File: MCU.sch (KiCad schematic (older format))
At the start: 36 parts, among them P1 CONN_02X05, P2 USB_OTG, SW48 Reset, U1 IS31FL3732, U2 MK20DX256VLH7, X1 CRYSTAL_SMD

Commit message: Reworked the Board
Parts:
- removed C13, C18, C19, C2, C3: 1uF, Capacitors_SMD:C_0603, symbol CP1
- removed C14, C15, C17, C20, C21, C4, C5, C6, C7: 0.1uF, Capacitors_SMD:C_0603, symbol CP1
- removed C8: 2.2uF, Capacitors_SMD:C_0603, symbol CP1
- removed D48: LED, LEDs:LED_0805, symbol LED
- removed P1: CONN_02X05, Pin_Headers:Pin_Header_Straight_2x05, symbol CONN_02X05
- removed P2: USB_OTG, Connect:USB_Micro-B, symbol USB_OTG
- removed SW48: Reset, mx2a:KSEM31GLFS, symbol SW_PUSH
- removed U1: IS31FL3732, Housings_DFN_QFN:UQFN-40-1EP_5x5mm_Pitch0.4mm, symbol IS31FL3732
- removed U2: MK20DX256VLH7, Housings_QFP:LQFP-64_10x10mm_Pitch0.5mm, symbol MK20DX256VLH7
- added C11, C13, C3, C6: 0.1uF, Capacitors_SMD:C_0603, symbol C
- added C2, C5, C7: 1uF, Capacitors_SMD:C_0603, symbol C
- added C4: 100uF, Capacitors_SMD:C_1206, symbol C
- added C8: 2.2uF, Capacitors_SMD:C_0603, symbol C
- added LED48: LED, lib.pretty:LED_0805, symbol LED
- added P1: USB_OTG, lib.pretty:Micro-USB_629105150521, symbol USB_OTG
- added P2, P3, P5: CONN_01X04, lib.pretty:Conn-4, symbol CONN_01X04
- added P4: FLASH_HDR, lib.pretty:JLINK_NEEDLE, symbol FLASH_HDR
- added P6, P7: CONN_01X02, lib.pretty:Conn-2, symbol CONN_01X02
- added R11: 100, Resistors_SMD:R_0603, symbol R
- added SW48: TAC_SWITCH, lib.pretty:PTS810, symbol TAC_SWITCH
- added U1: IS31FL3737, Housings_DFN_QFN:UQFN-40-1EP_5x5mm_Pitch0.4mm, symbol IS31FL3737
- added U2: MK20DX256VLH7-RESCUE-RainbowFox, Housings_QFP:LQFP-64_10x10mm_Pitch0.5mm, symbol MK20DX256VLH7-RESCUE-RainbowFox
- C1: value 100uF -> 0.1uF; footprint Capacitors_SMD:C_0805 -> Capacitors_SMD:C_0603
- C12: value 100n -> 0.1uF
- C9: value 2.2uF -> 0.1uF
- R1: value 1k -> 100k
- R3: value 33 -> 4.7k
- R4: value 33 -> 100k
- R5: value 5M -> 4.7k; footprint Resistors_SMD:R_0805 -> Resistors_SMD:R_0603
- R6: value 20k -> 33
- R7: value 1k -> 33
- R8: value 1k -> 20k
- R9: value 100k -> 5M; footprint Resistors_SMD:R_0603 -> Resistors_SMD:R_0805
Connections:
- net +3V3: now also C1.1, C9.1, R2.1, R3.1, R5.1, C11.1, C13.1, C2.1, C8.1, P4.1 (VCCS), U1.32 (VIO), U2.3 (VDD), U2.30 (VDD), U2.48 (VDD), U2.7 (VOUT33); no longer C9.2, R7.2, R8.2
- net +5V: now also C10.1, C3.1, C4.1, C5.1, C6.1, C7.1, P1.1 (VBUS), P2.1 (P1), P3.4 (P4), P4.5 (VKS), U1.19 (PVCC), U1.26 (PVCC), U1.31 (VCC), U2.8 (VREGIN); no longer C1.2, C10.2
- net D+: now also R7.1, U2.5 (USB0_DP); no longer R4.2
- net D-: now also R6.1, U2.6 (USB0_DM); no longer R3.2
- net GND: now also C1.2, C10.2, C9.2, R1.1, R4.1, R8.2, R9.2, C11.2, C13.2, C2.2, C3.2, C4.2, C5.2, C6.2, C7.2, P1.5 (GND), P2.4 (P4), P3.2 (P2), P4.3 (GND), SW48.4, U1.11 (PGND), U1.29 (AGND), U1.36 (ADDR), U1.4 (PGND), U1.40 (GND), U1.41 (Pad), U2.31 (VSS), U2.4 (VSS), U2.47 (VSS); no longer C1.1, C10.1, R1.2, R5.2, R6.1, R9.1
- net INTB: now also R2.2, P5.1 (P1), U1.37 (INTB), U2.40 (PTB17); no longer R2.1
- net MCU_RESET: now also P4.10 (RES), SW48.2, U2.34 (RESET_b)
- net PTA5: now also P4.9 (TRST), U2.27 (PTA5)
- net RX0: now also P4.8 (TDI), U2.23 (PTA1)
- net SCL: now also R3.2, P5.4 (P4), U1.35 (SCL), U2.35 (PTB0/LLWU_P5); no longer R7.1
- net SDA: now also R5.2, P5.3 (P3), U1.34 (SDA), U2.36 (PTB1); no longer R8.1
- net SDB: now also R1.2, P5.2 (P2), U1.38 (SDB), U2.39 (PTB16); no longer R9.2
- net SWD_CLK: now also R10.2, P3.3 (P3), P4.4 (TCK); no longer R10.1
- net TX0: now also P4.6 (TDO), U2.24 (PTA2/TRACE_SWD)
- net R_Ext renamed USB_D-
- net USB_D-: now also P1.2 (D-), P2.2 (P2)
- net X+: no longer names the net of X1.1
- net X+: now also U2.32 (EXTAL0/PTA18)
- net X-: no longer names the net of X1.2
- net X-: now also U2.33 (XDAL0/PTA19)
- new net: C8.2, R9.1
- new net: R11.1, U2.25 (PTA3/SWD_DIO)
- new net: R10.1, U2.22 (PTA0/SWD_CLK)
- new net: R4.2, U1.39 (IICRST)
- new net: R8.1, U1.30 (RSET)
- new net CS1: U1.15 (CS1)
- new net CS10: U1.25 (CS10)
- new net CS11: U1.27 (CS11)
- new net CS12: U1.28 (CS12)
- new net CS2: U1.16 (CS2)
- new net CS3: U1.17 (CS3)
- new net CS4: U1.18 (CS4)
- new net CS5: U1.20 (CS5)
- new net CS6: U1.21 (CS6)
- new net CS7: U1.22 (CS7)
- new net CS8: U1.23 (CS8)
- new net CS9: U1.24 (CS9)
- new net PTA12: U2.28 (PTA12)
- new net PTA13: U2.29 (PTA13/LLWU_P4)
- new net PTA4: U2.26 (PTA4/LLWU_P3)
- new net PTB18: U2.41 (PTB18)
- new net PTB19: U2.42 (PTB19)
- new net PTB2: U2.37 (PTB2)
- new net PTB3: U2.38 (PTB3)
- new net PTC0: U2.43 (PTC0)
- new net PTC1: U2.44 (PTC1/LLWU_P6)
- new net PTC10: U2.55 (PTC10)
- new net PTC11: U2.56 (PTC11/LLWU_P11)
- new net PTC2: U2.45 (PTC2)
- new net PTC3: U2.46 (PTC3/LLWU_P7)
- new net PTC4: U2.49 (PTC4/LLWU_P8)
- new net PTC5: U2.50 (PTC5/LLWU_P9)
- new net PTC6: U2.51 (PTC6/LLWU_P10)
- new net PTC7: U2.52 (PTC7)
- new net PTC8: U2.53 (PTC8)
- new net PTC9: U2.54 (PTC9)
- new net PTD0: U2.57 (PTD0/LLWU_P12)
- new net PTD1: U2.58 (PTD1)
- new net PTD4: U2.61 (PTD4/LLWU_P14)
- new net PTD5: U2.62 (PTD5)
- new net PTD6: U2.63 (PTD6/LLWU_P15)
- new net PTD7: U2.64 (PTD7)
- new net RX1: P7.1 (P1), U2.1 (PTE0)
- new net RX2: P6.1 (P1), U2.59 (PTD2/LLWU_P13)
- new net SW1: U1.1 (SW1)
- new net SW10: U1.12 (SW10)
- new net SW11: U1.13 (SW11)
- new net SW12: U1.14 (SW12)
- new net SW2: U1.2 (SW2)
- new net SW3: U1.3 (SW3)
- new net SW4: U1.5 (SW4)
- new net SW5: U1.6 (SW5)
- new net SW6: U1.7 (SW6)
- new net SW7: U1.8 (SW7)
- new net SW8: U1.9 (SW8)
- new net SW9: U1.10 (SW9)
- new net SWD_DIO: P3.1 (P1), P4.2 (TMS), R11.2
- new net TX1: P7.2 (P2), U2.2 (PTE1/LLWU_P0)
- new net TX2: P6.2 (P2), U2.60 (PTD3)
- new net USB_D+: P1.3 (D+), P2.3 (P3), R7.2
- no-connect marks 41 -> 19
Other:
- note added: "RESET internally\npulled high"

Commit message: Performed the changes from https://github.com/Project-Aurora/RainbowFox/commit/d956c5c3914152606eb0eeb9caeb00dc6e36fd84
Added Resistor to ground for firmware-LED
Connect VBAT to 3.3V
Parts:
- added R12: 1k, Resistors_SMD:R_0603, symbol R
- LED48: symbol LED -> LED-RESCUE-Brett-RGB
- P1: symbol USB_OTG -> USB_OTG-RESCUE-Brett-RGB
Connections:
- wire segments 116 -> 119
- no-connect marks 19 -> 18
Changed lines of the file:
@@
 EESchema Schematic File Version 2
+LIBS:Brett-RGB-rescue
 LIBS:power
 LIBS:device
@@
 encoding utf-8
 Sheet 2 2
-Title "RainbowFox"
-Date "2016-06-11"
-Rev "1.02a"
-Comp "Input Club"
+Title "Brett-RGB"
+Date ""
+Rev ""
+Comp ""
 Comment1 ""
 Comment2 ""
@@
 USB_D+
 $Comp
-L USB_OTG P1
+L USB_OTG-RESCUE-Brett-RGB P1
 U 1 1 575CA533
 P 750 1050
@@
 USB_D-
 $Comp
-L +5V #PWR01
+L +5V #PWR2
 U 1 1 575CB90E
 P 2050 850
-F 0 "#PWR01" H 2050 700 50  0001 C CNN
+F 0 "#PWR2" H 2050 700 50  0001 C CNN
 F 1 "+5V" H 2050 990 50  0000 C CNN
 F 2 "" H 2050 850 50  0000 C CNN
@@
 $EndComp
 $Comp
-L GND #PWR02
+L GND #PWR6
 U 1 1 575CB946
 P 2900 1250
-F 0 "#PWR02" H 2900 1000 50  0001 C CNN
+F 0 "#PWR6" H 2900 1000 50  0001 C CNN
 F 1 "GND" H 2900 1100 50  0000 C CNN
 F 2 "" H 2900 1250 50  0000 C CNN
@@
 $EndComp
 $Comp
-L GND #PWR03
+L GND #PWR27
 U 1 1 575D1056
-P 6550 5750
-F 0 "#PWR03" H 6550 5500 50  0001 C CNN
-F 1 "GND" H 6550 5600 50  0000 C CNN
-F 2 "" H 6550 5750 50  0000 C CNN
-F 3 "" H 6550 5750 50  0000 C CNN
-	1    6550 5750
+P 6550 6050
+F 0 "#PWR27" H 6550 5800 50  0001 C CNN
+F 1 "GND" H 6550 5900 50  0000 C CNN
+F 2 "" H 6550 6050 50  0000 C CNN
+F 3 "" H 6550 6050 50  0000 C CNN
+	1    6550 6050
 	1    0    0    -1
 $EndComp
@@
 NoConn ~ 4900 3150
 NoConn ~ 4900 3050
-NoConn ~ 6050 4500
-$Comp
-L LED LED48
+$Comp
+L LED-RESCUE-Brett-RGB LED48
 U 1 1 575C7327
 P 6550 5550
+AR Path="/575C7327" Ref="LED48"  Part="1"
+AR Path="/573CCE5B/575C7327" Ref="LED48"  Part="1"
 F 0 "LED48" H 6550 5650 50  0000 C CNN
 F 1 "LED" H 6550 5450 50  0000 C CNN
@@
 $EndComp
 $Comp
-L GND #PWR04
+L GND #PWR20
 U 1 1 575C7BBF
 P 7600 4800
-F 0 "#PWR04" H 7600 4550 50  0001 C CNN
+F 0 "#PWR20" H 7600 4550 50  0001 C CNN
 F 1 "GND" H 7600 4650 50  0000 C CNN
 F 2 "" H 7600 4800 50  0000 C CNN
@@
 $EndComp
 $Comp
-L GND #PWR05
+L GND #PWR24
 U 1 1 575C810A
 P 7250 5150
-F 0 "#PWR05" H 7250 4900 50  0001 C CNN
+F 0 "#PWR24" H 7250 4900 50  0001 C CNN
 F 1 "GND" H 7250 5000 50  0000 C CNN
 F 2 "" H 7250 5150 50  0000 C CNN
@@
 $EndComp
 $Comp
-L GND #PWR06
+L GND #PWR17
 U 1 1 575C868D
 P 9050 3850
-F 0 "#PWR06" H 9050 3600 50  0001 C CNN
+F 0 "#PWR17" H 9050 3600 50  0001 C CNN
 F 1 "GND" H 9050 3700 50  0000 C CNN
 F 2 "" H 9050 3850 50  0000 C CNN
@@
 $EndComp
 $Comp
-L GND #PWR07
+L GND #PWR18
 U 1 1 575C9201
 P 8050 4100
-F 0 "#PWR07" H 8050 3850 50  0001 C CNN
+F 0 "#PWR18" H 8050 3850 50  0001 C CNN
 F 1 "GND" H 8050 3950 50  0000 C CNN
 F 2 "" H 8050 4100 50  0000 C CNN
@@
 $EndComp
 $Comp
-L GND #PWR08
+L GND #PWR12
 U 1 1 575C9D7B
 P 8400 2350
-F 0 "#PWR08" H 8400 2100 50  0001 C CNN
+F 0 "#PWR12" H 8400 2100 50  0001 C CNN
 F 1 "GND" H 8400 2200 50  0000 C CNN
 F 2 "" H 8400 2350 50  0000 C CNN
@@
 $EndComp
 $Comp
-L +3.3V #PWR09
+L +3.3V #PWR10
 U 1 1 575CA307
 P 8150 2050
-F 0 "#PWR09" H 8150 1900 50  0001 C CNN
+F 0 "#PWR10" H 8150 1900 50  0001 C CNN
 F 1 "+3.3V" H 8150 2190 50  0000 C CNN
 F 2 "" H 8150 2050 50  0000 C CNN
@@
 $EndComp
 $Comp
-L GND #PWR010
+L GND #PWR13
 U 1 1 575CA5B6
 P 4400 2550
-F 0 "#PWR010" H 4400 2300 50  0001 C CNN
+F 0 "#PWR13" H 4400 2300 50  0001 C CNN
 F 1 "GND" H 4400 2400 50  0000 C CNN
 F 2 "" H 4400 2550 50  0000 C CNN
@@
 $EndComp
 $Comp
-L +3.3V #PWR011
+L +3.3V #PWR11
 U 1 1 575CAD2D
 P 4400 2250
-F 0 "#PWR011" H 4400 2100 50  0001 C CNN
+F 0 "#PWR11" H 4400 2100 50  0001 C CNN
 F 1 "+3.3V" H 4400 2390 50  0000 C CNN
 F 2 "" H 4400 2250 50  0000 C CNN
@@
 $EndComp
 $Comp
-L +3.3V #PWR012
+L +3.3V #PWR23
 U 1 1 575CB558
 P 6950 5150
-F 0 "#PWR012" H 6950 5000 50  0001 C CNN
+F 0 "#PWR23" H 6950 5000 50  0001 C CNN
 F 1 "+3.3V" H 6950 5290 50  0000 C CNN
 F 2 "" H 6950 5150 50  0000 C CNN
@@
 $EndComp
 $Comp
-L GND #PWR013
+L GND #PWR16
 U 1 1 575CD528
 P 4400 3550
-F 0 "#PWR013" H 4400 3300 50  0001 C CNN
+F 0 "#PWR16" H 4400 3300 50  0001 C CNN
 F 1 "GND" H 4400 3400 50  0000 C CNN
 F 2 "" H 4400 3550 50  0000 C CNN
@@
 $EndComp
 $Comp
-L +3.3V #PWR014
+L +3.3V #PWR14
 U 1 1 575CD770
 P 4200 2850
-F 0 "#PWR014" H 4200 2700 50  0001 C CNN
+F 0 "#PWR14" H 4200 2700 50  0001 C CNN
 F 1 "+3.3V" H 4200 2990 50  0000 C CNN
 F 2 "" H 4200 2850 50  0000 C CNN
@@
 $EndComp
 $Comp
-L +5V #PWR015
+L +5V #PWR15
 U 1 1 575CD8E4
 P 4550 2950
-F 0 "#PWR015" H 4550 2800 50  0001 C CNN
+F 0 "#PWR15" H 4550 2800 50  0001 C CNN
 F 1 "+5V" H 4550 3090 50  0000 C CNN
 F 2 "" H 4550 2950 50  0000 C CNN
@@
 $EndComp
 $Comp
-L +3.3V #PWR016
+L +3.3V #PWR1
 U 1 1 575D0650
 P 9800 750
-F 0 "#PWR016" H 9800 600 50  0001 C CNN
+F 0 "#PWR1" H 9800 600 50  0001 C CNN
 F 1 "+3.3V" H 9800 890 50  0000 C CNN
 F 2 "" H 9800 750 50  0000 C CNN
@@
 $EndComp
 $Comp
-L GND #PWR017
+L GND #PWR8
 U 1 1 575D069B
 P 9600 1450
-F 0 "#PWR017" H 9600 1200 50  0001 C CNN
+F 0 "#PWR8" H 9600 1200 50  0001 C CNN
 F 1 "GND" H 9600 1300 50  0000 C CNN
 F 2 "" H 9600 1450 50  0000 C CNN
@@
 $EndComp
 $Comp
-L +5V #PWR018
+L +5V #PWR9
 U 1 1 575D1514
 P 9800 1450
-F 0 "#PWR018" H 9800 1300 50  0001 C CNN
+F 0 "#PWR9" H 9800 1300 50  0001 C CNN
 F 1 "+5V" H 9800 1590 50  0000 C CNN
 F 2 "" H 9800 1450 50  0000 C CNN
@@
 USB_D-
 $Comp
-L +5V #PWR019
+L +5V #PWR3
 U 1 1 575E7A49
 P 2900 850
-F 0 "#PWR019" H 2900 700 50  0001 C CNN
+F 0 "#PWR3" H 2900 700 50  0001 C CNN
 F 1 "+5V" H 2900 990 50  0000 C CNN
 F 2 "" H 2900 850 50  0000 C CNN
@@
 $EndComp
 $Comp
-L GND #PWR020
+L GND #PWR5
 U 1 1 575E7A8D
 P 2050 1250
-F 0 "#PWR020" H 2050 1000 50  0001 C CNN
+F 0 "#PWR5" H 2050 1000 50  0001 C CNN
 F 1 "GND" H 2050 1100 50  0000 C CNN
 F 2 "" H 2050 1250 50  0000 C CNN
@@
 $EndComp
 $Comp
-L +5V #PWR021
+L +5V #PWR7
 U 1 1 57883411
 P 3700 1250
-F 0 "#PWR021" H 3700 1100 50  0001 C CNN
+F 0 "#PWR7" H 3700 1100 50  0001 C CNN
 F 1 "+5V" H 3700 1390 50  0000 C CNN
 F 2 "" H 3700 1250 50  0000 C CNN
@@
 SWD_CLK
 $Comp
-L GND #PWR022
+L GND #PWR4
 U 1 1 57884050
 P 3550 1000
-F 0 "#PWR022" H 3550 750 50  0001 C CNN
+F 0 "#PWR4" H 3550 750 50  0001 C CNN
 F 1 "GND" H 3550 850 50  0000 C CNN
 F 2 "" H 3550 1000 50  0000 C CNN
@@
 Connection ~ 1400 5200
 $Comp
-L GND #PWR023
+L GND #PWR21
 U 1 1 5785F291
 P 1300 5150
-F 0 "#PWR023" H 1300 4900 50  0001 C CNN
+F 0 "#PWR21" H 1300 4900 50  0001 C CNN
 F 1 "GND" H 1300 5000 50  0000 C CNN
 F 2 "" H 1300 5150 50  0000 C CNN
@@
 Connection ~ 1150 6300
 $Comp
-L +3.3V #PWR024
+L +3.3V #PWR29
 U 1 1 57861E36
 P 1100 6300
-F 0 "#PWR024" H 1100 6150 50  0001 C CNN
+F 0 "#PWR29" H 1100 6150 50  0001 C CNN
 F 1 "+3.3V" H 1100 6440 50  0000 C CNN
 F 2 "" H 1100 6300 50  0000 C CNN
@@
 $EndComp
 $Comp
-L GND #PWR025
+L GND #PWR26
 U 1 1 57861EB8
 P 1400 5800
-F 0 "#PWR025" H 1400 5550 50  0001 C CNN
+F 0 "#PWR26" H 1400 5550 50  0001 C CNN
 F 1 "GND" H 1400 5650 50  0000 C CNN
 F 2 "" H 1400 5800 50  0000 C CNN
@@
 Connection ~ 1250 6600
 $Comp
-L GND #PWR026
+L GND #PWR31
 U 1 1 57862C8E
 P 1250 6650
-F 0 "#PWR026" H 1250 6400 50  0001 C CNN
+F 0 "#PWR31" H 1250 6400 50  0001 C CNN
 F 1 "GND" H 1250 6500 50  0000 C CNN
 F 2 "" H 1250 6650 50  0000 C CNN
@@
 Connection ~ 1750 6900
 $Comp
-L +5V #PWR027
+L +5V #PWR32
 U 1 1 57863C08
 P 1550 6950
-F 0 "#PWR027" H 1550 6800 50  0001 C CNN
+F 0 "#PWR32" H 1550 6800 50  0001 C CNN
 F 1 "+5V" H 1550 7090 50  0000 C CNN
 F 2 "" H 1550 6950 50  0000 C CNN
@@
 	1950 7200 1950 7250
 $Comp
-L GND #PWR028
+L GND #PWR34
 U 1 1 578644F8
 P 1950 7250
-F 0 "#PWR028" H 1950 7000 50  0001 C CNN
+F 0 "#PWR34" H 1950 7000 50  0001 C CNN
 F 1 "GND" H 1950 7100 50  0000 C CNN
 F 2 "" H 1950 7250 50  0000 C CNN
@@
 $EndComp
 $Comp
-L +5V #PWR029
+L +5V #PWR33
 U 1 1 57865610
 P 2550 7000
-F 0 "#PWR029" H 2550 6850 50  0001 C CNN
+F 0 "#PWR33" H 2550 6850 50  0001 C CNN
 F 1 "+5V" H 2550 7140 50  0000 C CNN
 F 2 "" H 2550 7000 50  0000 C CNN
@@
 $EndComp
 $Comp
-L +5V #PWR030
+L +5V #PWR28
 U 1 1 57866E1E
 P 4350 6250
-F 0 "#PWR030" H 4350 6100 50  0001 C CNN
+F 0 "#PWR28" H 4350 6100 50  0001 C CNN
 F 1 "+5V" H 4350 6390 50  0000 C CNN
 F 2 "" H 4350 6250 50  0000 C CNN
@@
 	3900 6450 4100 6450
 $Comp
-L GND #PWR031
+L GND #PWR30
 U 1 1 57867905
 P 4100 6450
-F 0 "#PWR031" H 4100 6200 50  0001 C CNN
+F 0 "#PWR30" H 4100 6200 50  0001 C CNN
 F 1 "GND" H 4100 6300 50  0000 C CNN
 F 2 "" H 4100 6450 50  0000 C CNN
@@
 $EndComp
 $Comp
-L GND #PWR032
+L GND #PWR19
 U 1 1 578688A9
 P 2400 4550
-F 0 "#PWR032" H 2400 4300 50  0001 C CNN
+F 0 "#PWR19" H 2400 4300 50  0001 C CNN
 F 1 "GND" H 2400 4400 50  0000 C CNN
 F 2 "" H 2400 4550 50  0000 C CNN
@@
 $EndComp
 $Comp
-L GND #PWR033
+L GND #PWR25
 U 1 1 57868B06
 P 3750 5350
-F 0 "#PWR033" H 3750 5100 50  0001 C CNN
+F 0 "#PWR25" H 3750 5100 50  0001 C CNN
 F 1 "GND" H 3750 5200 50  0000 C CNN
 F 2 "" H 3750 5350 50  0000 C CNN
@@
 Text Label 4900 2350 2    39   ~ 0
 TX1
+Text Label 4850 1100 2    39   ~ 0
+RX1
 Text Label 4850 1000 2    39   ~ 0
-RX1
-Text Label 4850 1100 2    39   ~ 0
 TX1
+$Comp
+L +3.3V #PWR22
+U 1 1 587DA6DA
+P 5950 5150
+F 0 "#PWR22" H 5950 5000 50  0001 C CNN
+F 1 "+3.3V" H 5950 5290 50  0000 C CNN
+F 2 "" H 5950 5150 50  0000 C CNN
+F 3 "" H 5950 5150 50  0000 C CNN
+	1    5950 5150
+	-1   0    0    1
+$EndComp
+Wire Wire Line
+	6050 4500 6050 4800
+Wire Wire Line
+	6050 4800 5950 4800
+Wire Wire Line
+	5950 4800 5950 5150
+$Comp
+L R R12
+U 1 1 587DBA44
+P 6550 5900
+F 0 "R12" V 6630 5900 50  0000 C CNN
+F 1 "1k" V 6550 5900 50  0000 C CNN
+F 2 "Resistors_SMD:R_0603" V 6480 5900 50  0001 C CNN
+F 3 "" H 6550 5900 50  0000 C CNN
+	1    6550 5900
+	1    0    0    -1
+$EndComp
 $EndSCHEMATC

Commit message: Added Pinout for 3.3V
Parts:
- removed LED48: LED, lib.pretty:LED_0805, symbol LED-RESCUE-Brett-RGB
- removed P1: USB_OTG, lib.pretty:Micro-USB_629105150521, symbol USB_OTG-RESCUE-Brett-RGB
- removed P3: CONN_01X04, lib.pretty:Conn-4, symbol CONN_01X04
- added LED48: LED, lib.pretty:LED_0805, symbol LED
- added P1: USB_OTG, lib.pretty:Micro-USB_629105150521, symbol USB_OTG
- added P3: CONN_01X05, lib.pretty:Conn-5, symbol CONN_01X05
- C1: footprint Capacitors_SMD:C_0603 -> lib.pretty:LED_0805
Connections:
- wire segments 119 -> 123

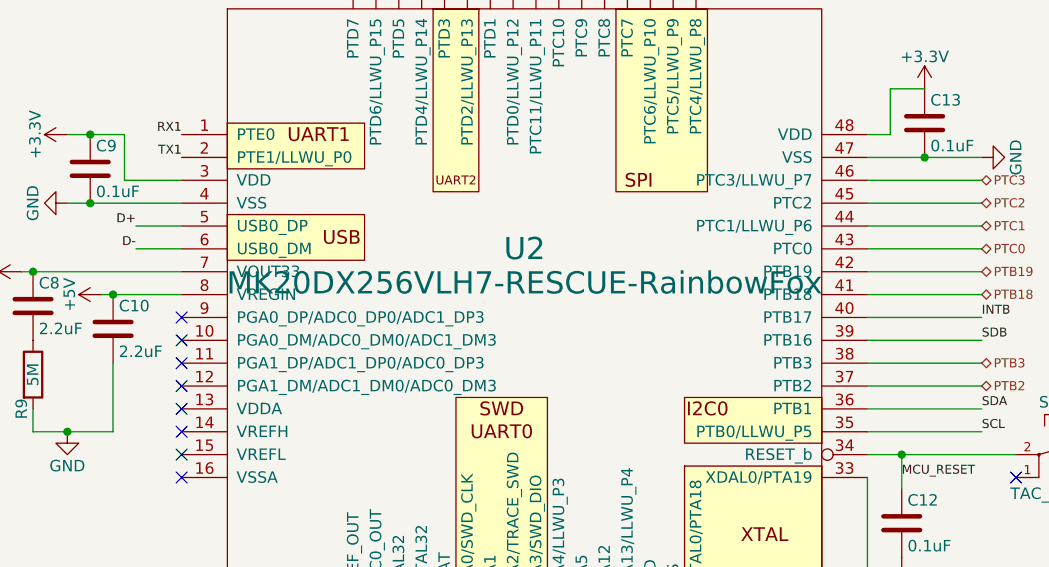
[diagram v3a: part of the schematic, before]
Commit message: Fixed MCU name in Schematic
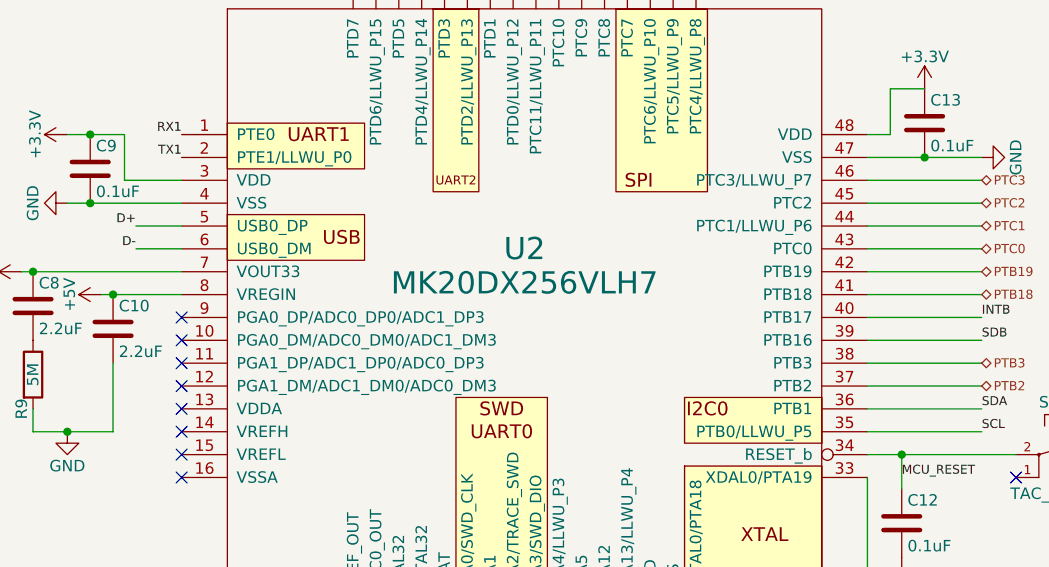
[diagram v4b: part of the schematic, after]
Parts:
- removed U2: MK20DX256VLH7-RESCUE-RainbowFox, Housings_QFP:LQFP-64_10x10mm_Pitch0.5mm, symbol MK20DX256VLH7-RESCUE-RainbowFox
- added U2: MK20DX256VLH7, symbol MK20DX256VLH7
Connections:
- net +3V3: now also U2.21 (VBAT), U2.3 (VDD), U2.30 (VDD), U2.48 (VDD), U2.7 (VOUT33)
- net +5V: now also U2.8 (VREGIN)
- net D+: now also U2.5 (USB0_DP)
- net D-: now also U2.6 (USB0_DM)
- net GND: now also U2.31 (VSS), U2.4 (VSS), U2.47 (VSS)
- net INTB: now also U2.40 (PTB17)
- net MCU_RESET: now also U2.34 (RESET_b)
- net PTA12: now also U2.28 (PTA12)
- net PTA13: now also U2.29 (PTA13/LLWU_P4)
- net PTA4: now also U2.26 (PTA4/LLWU_P3)
- net PTA5: now also U2.27 (PTA5)
- net PTB18: now also U2.41 (PTB18)
- net PTB19: now also U2.42 (PTB19)
- net PTB2: now also U2.37 (PTB2)
- net PTB3: now also U2.38 (PTB3)
- net PTC0: now also U2.43 (PTC0)
- net PTC1: now also U2.44 (PTC1/LLWU_P6)
- net PTC10: now also U2.55 (PTC10)
- net PTC11: now also U2.56 (PTC11/LLWU_P11)
- net PTC2: now also U2.45 (PTC2)
- net PTC3: now also U2.46 (PTC3/LLWU_P7)
- net PTC4: now also U2.49 (PTC4/LLWU_P8)
- net PTC5: now also U2.50 (PTC5/LLWU_P9)
- net PTC6: now also U2.51 (PTC6/LLWU_P10)
- net PTC7: now also U2.52 (PTC7)
- net PTC8: now also U2.53 (PTC8)
- net PTC9: now also U2.54 (PTC9)
- net PTD0: now also U2.57 (PTD0/LLWU_P12)
- net PTD1: now also U2.58 (PTD1)
- net PTD4: now also U2.61 (PTD4/LLWU_P14)
- net PTD5: now also U2.62 (PTD5)
- net PTD6: now also U2.63 (PTD6/LLWU_P15)
- net PTD7: now also U2.64 (PTD7)
- net RX0: now also U2.23 (PTA1)
- net RX1: now also U2.1 (PTE0)
- net RX2: now also U2.59 (PTD2/LLWU_P13)
- net SCL: now also U2.35 (PTB0/LLWU_P5)
- net SDA: now also U2.36 (PTB1)
- net SDB: now also U2.39 (PTB16)
- net TX0: now also U2.24 (PTA2/TRACE_SWD)
- net TX1: now also U2.2 (PTE1/LLWU_P0)
- net TX2: now also U2.60 (PTD3)
- net at X1.1: now also U2.32 (EXTAL0/PTA18)
- net at X1.2: now also U2.33 (XDAL0/PTA19)
- net at R11.1: now also U2.25 (PTA3/SWD_DIO)
- net at R10.1: now also U2.22 (PTA0/SWD_CLK)
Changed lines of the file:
@@
 	1650 1050 1600 1050
-$Comp
-L MK20DX256VLH7-RESCUE-RainbowFox U2
-U 1 1 57864E3F
-P 6400 3000
-F 0 "U2" H 6400 3250 97  0000 C CNN
-F 1 "MK20DX256VLH7-RESCUE-RainbowFox" H 6400 3100 97  0000 C CNN
-F 2 "Housings_QFP:LQFP-64_10x10mm_Pitch0.5mm" H 6400 3000 60  0001 C CNN
-F 3 "" H 6400 3000 60  0000 C CNN
-	1    6400 3000
-	1    0    0    -1
-$EndComp
 $Comp
 L FLASH_HDR P4
@@
 Wire Wire Line
 	3700 1250 3700 1300
+$Comp
+L MK20DX256VLH7 U2
+U 1 1 58ACAF7D
+P 6400 3000
+F 0 "U2" H 6400 3250 97  0000 C CNN
+F 1 "MK20DX256VLH7" H 6400 3100 97  0000 C CNN
+F 2 "" H 6400 3000 60  0000 C CNN
+F 3 "" H 6400 3000 60  0000 C CNN
+	1    6400 3000
+	1    0    0    -1
+$EndComp
 $EndSCHEMATC
